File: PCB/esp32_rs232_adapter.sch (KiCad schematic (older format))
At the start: 41 parts, among them J2 DB9, J3 Shunt-, J4 Poles, J5 Common, J6 Shunt+, SW1 Flash, SW2 Null_Modem_Selector, U1 ESP32-WROOM-32D, U2 MAX3232, U5 ACS712xLCTR-30A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

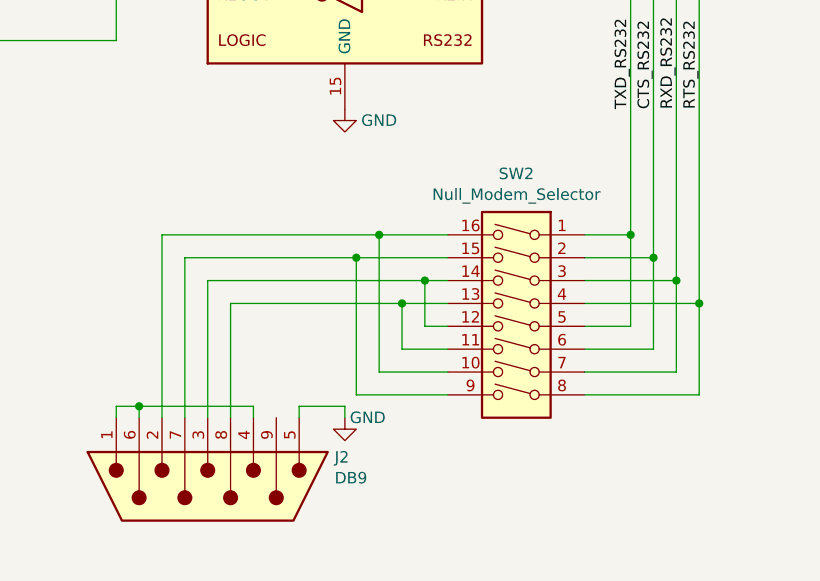
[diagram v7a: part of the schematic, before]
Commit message: remove null modem switch
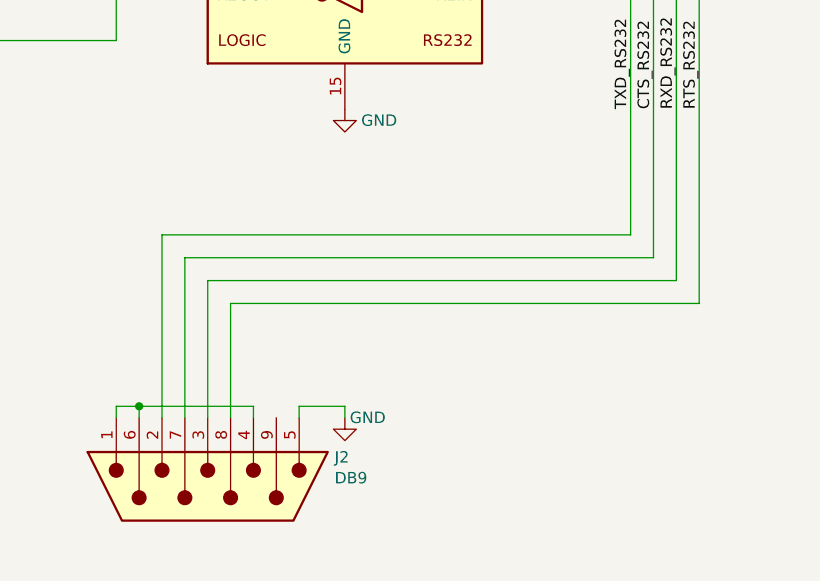
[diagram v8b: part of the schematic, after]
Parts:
- removed SW2: Null_Modem_Selector, Button_Switch_SMD:SW_DIP_SPSTx08_Slide_6.7x21.88mm_W8.61mm_P2.54mm_LowProfile, symbol Switch:SW_DIP_x08
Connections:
- wire segments 194 -> 170
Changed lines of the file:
@@
 EESchema Schematic File Version 4
 LIBS:esp32_rs232_adapter-cache
-EELAYER 26 0
+EELAYER 29 0
 EELAYER END
 $Descr A4 11693 8268
@@
 	0    -1   -1   0
 $EndComp
-$Comp
-L Switch:SW_DIP_x08 SW2
-U 1 1 5C88E389
-P 9950 4550
-F 0 "SW2" H 9950 5217 50  0000 C CNN
-F 1 "Null_Modem_Selector" H 9950 5126 50  0000 C CNN
-F 2 "Button_Switch_SMD:SW_DIP_SPSTx08_Slide_6.7x21.88mm_W8.61mm_P2.54mm_LowProfile" H 9950 4550 50  0001 C CNN
-F 3 "https://www.aliexpress.com/item/10pcs-lot-Slide-Type-SMT-SMD-Dip-Switch-2-54mm-Pitch-2-Row-4-Pin-2/32956815576.html" H 9950 4550 50  0001 C CNN
-	1    9950 4550
-	-1   0    0    -1
-$EndComp
-Wire Wire Line
-	10450 4150 10250 4150
-Wire Wire Line
-	9650 4150 9350 4150
-Wire Wire Line
-	10450 2500 10450 4150
-Wire Wire Line
-	10450 4150 10450 4550
-Wire Wire Line
-	10450 4550 10250 4550
-Connection ~ 10450 4150
-Wire Wire Line
-	10550 4250 10250 4250
-Wire Wire Line
-	10550 4250 10550 4650
-Wire Wire Line
-	10550 4650 10250 4650
-Connection ~ 10550 4250
-Wire Wire Line
-	10650 4350 10250 4350
-Wire Wire Line
-	10650 4350 10650 4750
-Wire Wire Line
-	10650 4750 10250 4750
-Connection ~ 10650 4350
-Wire Wire Line
-	10750 4450 10250 4450
-Wire Wire Line
-	10750 4450 10750 4850
-Wire Wire Line
-	10750 4850 10250 4850
-Connection ~ 10750 4450
-Wire Wire Line
-	9650 4250 9250 4250
 Wire Wire Line
 	8500 4250 8500 4950
-Wire Wire Line
-	10550 3100 10550 4250
-Wire Wire Line
-	9650 4350 9550 4350
-Wire Wire Line
-	10650 2900 10650 4350
-Wire Wire Line
-	9650 4450 9450 4450
-Wire Wire Line
-	10750 2700 10750 4450
-Wire Wire Line
-	9650 4550 9550 4550
-Wire Wire Line
-	9550 4550 9550 4350
-Connection ~ 9550 4350
-Wire Wire Line
-	9550 4350 8600 4350
-Wire Wire Line
-	9650 4750 9350 4750
-Wire Wire Line
-	9350 4750 9350 4150
-Connection ~ 9350 4150
-Wire Wire Line
-	9350 4150 8400 4150
-Wire Wire Line
-	9650 4650 9450 4650
-Wire Wire Line
-	9450 4650 9450 4450
-Connection ~ 9450 4450
-Wire Wire Line
-	9450 4450 8700 4450
-Wire Wire Line
-	9650 4850 9250 4850
-Wire Wire Line
-	9250 4850 9250 4250
-Connection ~ 9250 4250
-Wire Wire Line
-	9250 4250 8500 4250
 $Comp
 L Mechanical:MountingHole H?
@@
 	-1   0    0    1
 $EndComp
+Wire Wire Line
+	10750 2700 10750 4450
+Wire Wire Line
+	10650 2900 10650 4350
+Wire Wire Line
+	10550 3100 10550 4250
+Wire Wire Line
+	10450 2500 10450 4150
+Wire Wire Line
+	8400 4150 10450 4150
+Wire Wire Line
+	8500 4250 10550 4250
+Wire Wire Line
+	8600 4350 10650 4350
+Wire Wire Line
+	8700 4450 10750 4450
 $EndSCHEMATC
